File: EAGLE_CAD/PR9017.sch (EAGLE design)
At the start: 74 parts, among them SW1 C&K_PTS645, Y1 ABS25XTAL

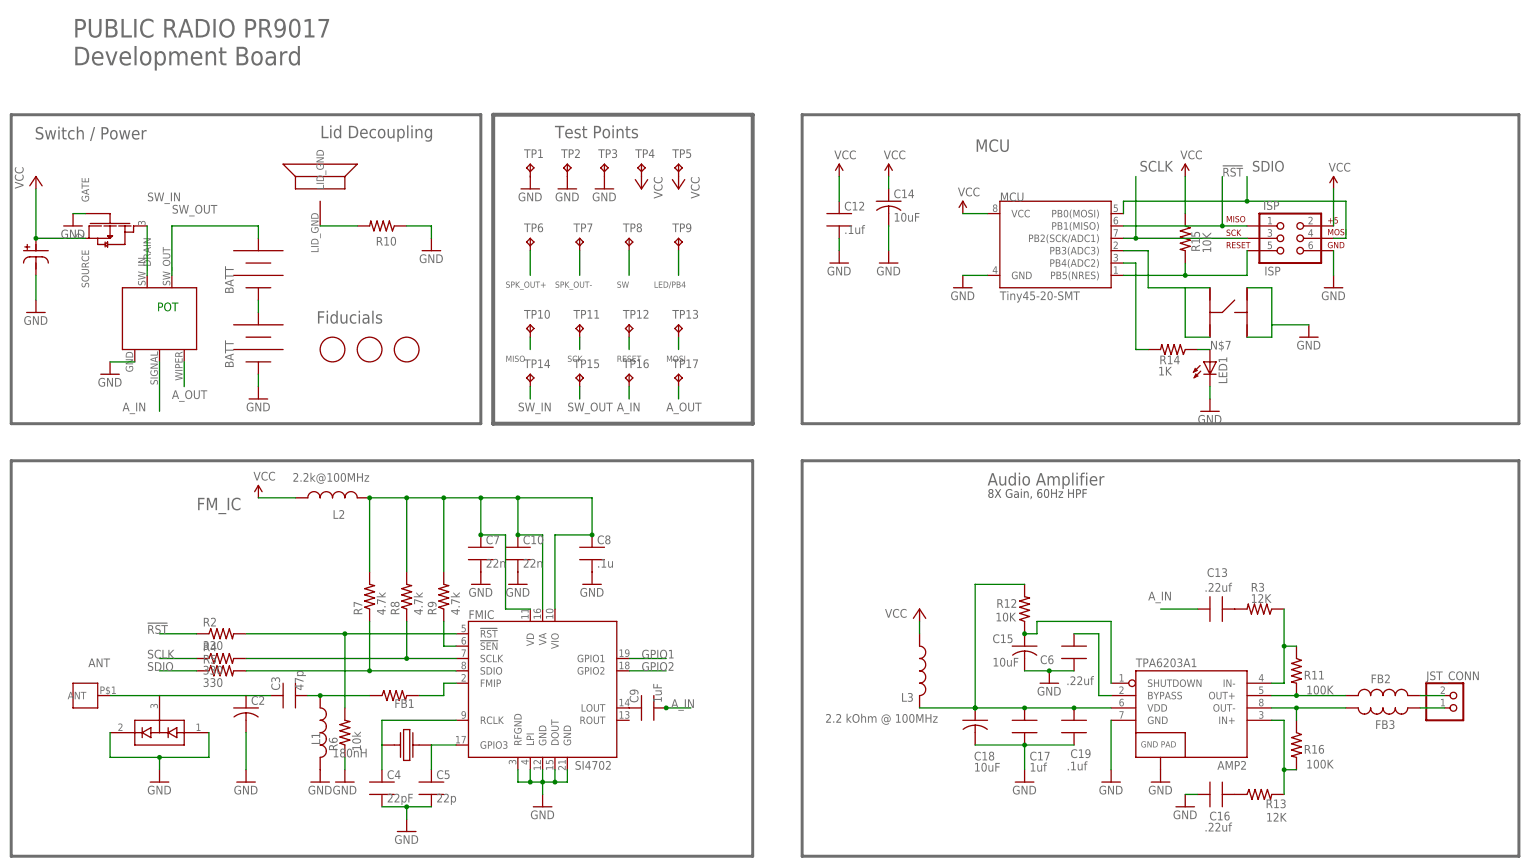
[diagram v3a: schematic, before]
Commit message: okay, woah
i spent a *ton* of time going through the partlist & BOM. at this point
basically everything in the circuit is from our PR_Parts_Library. i
also simplified & improved the package names, descriptions, etc. and i
gave all the passives 0603 footprints that came from the Common Parts
Library.

big thing: the values @ manufacturer part numbers. all of our parts
have a custom attribute called “MFG_PN”. we should go through EVERY
PART ON OUR SCHEMATIC and put actual manufacturer part numbers in those
fields. i did this for all the parts that seemed critical, but i didn’t
touch passives at all.

there’s also some other stuff that will matter on the BOM/partlist
side, but it’s probably best to just walk through in person or
digitally.

then: i went through all the parts and actually made them 0603.

then: i played with the FMIC area a bit. it’s not perfect but it’s a
start.

then: i started laying out the amp section. that’s definitely not done.
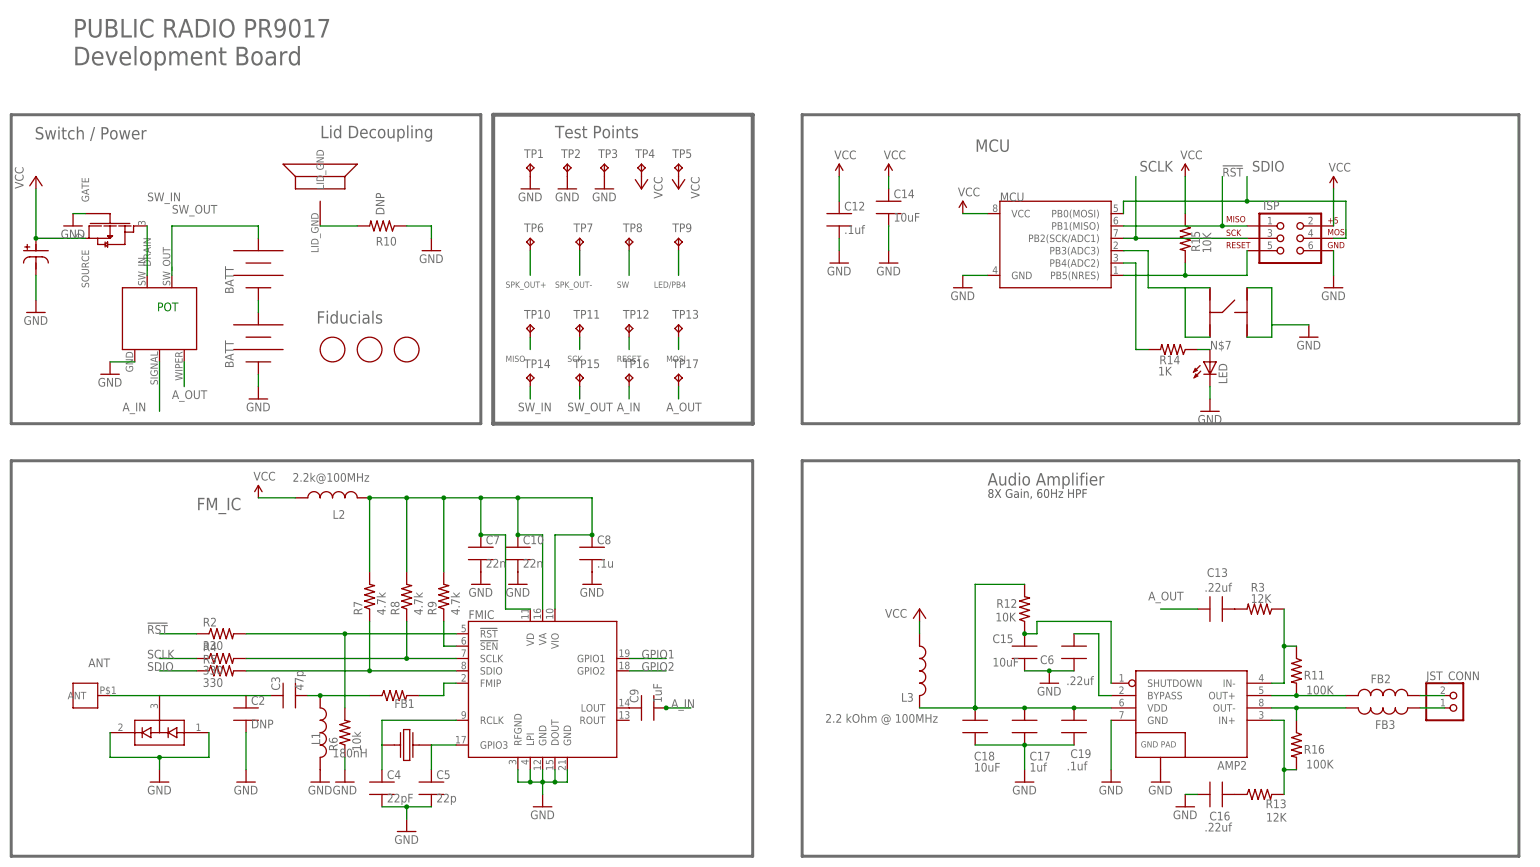
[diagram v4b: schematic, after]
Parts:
- removed LED1: (no value), led:LEDSML0603
- added LED: LED, PR_Parts_Library:LED
- ANT_MOUNT: value M3_SCREW_POST -> DNP
- C10, C12, C13, C16, C17, C19, C3, C4, C5, C6, C7, C8, C9: device PR_Parts_Library:CAP_SMT -> PR_Parts_Library:C_SMT_0603_CPL
- C14, C15, C18: device resistor:C-USC0603 -> PR_Parts_Library:C_SMT_0603_CPL
- C2: value (none) -> DNP; device resistor:C-USC0805 -> PR_Parts_Library:C_SMT_0603_CPL
- D1: device SparkFun-DiscreteSemi:BAV99 -> PR_Parts_Library:BAV99; MFG_PN (none) -> BAV99,215
- FB1, R6: device resistor:R-US_R0402 -> PR_Parts_Library:R_SMT_R0603_CPL
- FB2, FB3, L1: device SparkFun-Passives:INDUCTOR0805 -> PR_Parts_Library:L_SMT_0805_ADAFRUIT
- FET1: MFG_PN (none) -> AO3435
- FMIC: value SI4702 -> SI4702-C19-GMR; device PR_Parts_Library:SI470X -> PR_Parts_Library:SI4702-C19-GMR
- ISP: value ISP -> AVR_SPI_PRG_6NS; device SparkFun-Connectors:AVR_SPI_PRG_6NS -> PR_Parts_Library:AVR_SPI_PRG_6NS
- JST_CONN: device adafruit:JST_2PIN-SMT-RA -> PR_Parts_Library:JST_2PIN-SMT-RA
- L2, L3: device PR_Parts_Library:INDUCTOR -> PR_Parts_Library:L_SMT_0603_CPL
- MARK1, MARK2, MARK3: device adafruit:FIDUCIAL -> PR_Parts_Library:FIDUCIAL
- MCU: value Tiny45-20-SMT -> (none); device SparkFun-DigitalIC:ATTINY45TINY85-20-SMT -> PR_Parts_Library:ATTINY45TINY45-20-SMT
- R10: value (none) -> DNP; device resistor:R-US_R0805 -> PR_Parts_Library:R_SMT_R0603_CPL
- R11, R12, R13, R14, R15, R16, R2, R3, R4, R5, R7, R8, R9: device PR_Parts_Library:RES_SMT -> PR_Parts_Library:R_SMT_R0603_CPL
- SPKR_PLACE: value (none) -> DNP; device PR_Parts_Library:CE32A_FOR_JST -> PR_Parts_Library:PR2023_SPKR
- TP1, TP10, TP11, TP12, TP13, TP14, TP15, TP16, TP17, TP2, TP3, TP4, TP5, TP6, TP7, TP8, TP9: value TPTP20R -> (none); device testpad:TPTP20R -> PR_Parts_Library:TPTP20R
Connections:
- net A_IN: no longer C13.1
- net A_OUT: now also C13.1
- net GND: now also LED.C; no longer LED1.C
- net N$7: now also LED.A; no longer LED1.A

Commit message: Amp Updates
Changed the layout
-moved the decoupling as close as possible to the vd pin
-kept bypass cap also close by
-rerouted power
-removed the cap to ground on the shutdown pin from out previous
design, was not in place on any of the documentation for the 6203.
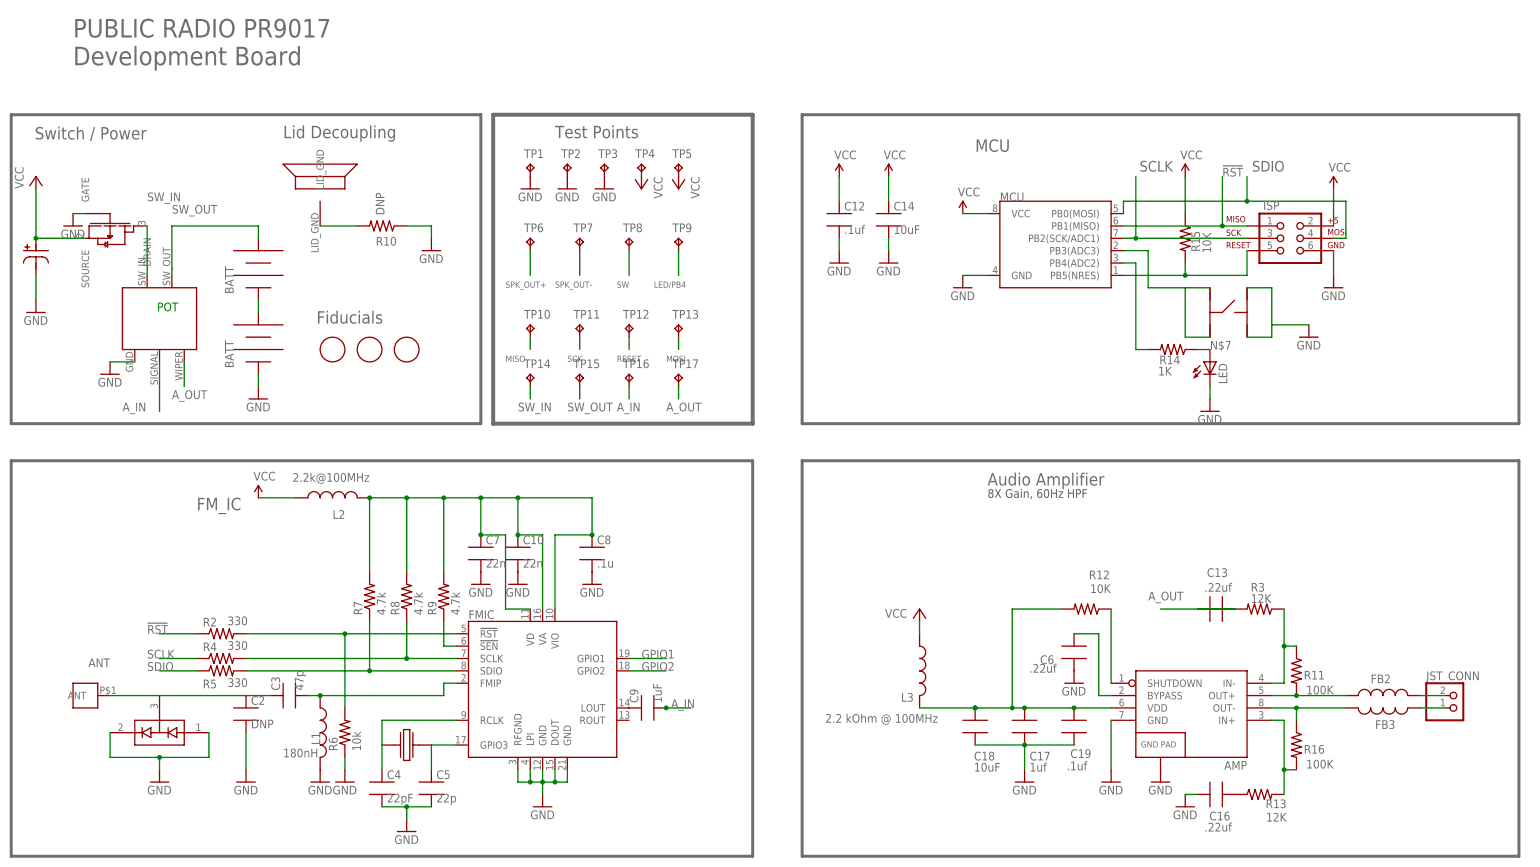
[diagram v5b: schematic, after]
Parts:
- removed C15: 10uF, PR_Parts_Library:C_SMT_0603_CPL
- removed FB1: (no value), PR_Parts_Library:R_SMT_R0603_CPL
- renumbered AMP2 to AMP
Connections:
- net A_OUT: now also C13.2; no longer C13.1
- net GND: no longer C15.2
- net N$16: no longer FB1.1
- net N$20: no longer C15.1
- net N$3: now also C13.1; no longer C13.2
- net N$6: no longer FB1.2
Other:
- moved on the sheet: C14, R12

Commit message: updated all part number etc
part number
added attributes for tolerance, voltage, power, etc
re routed FMIC per AN383
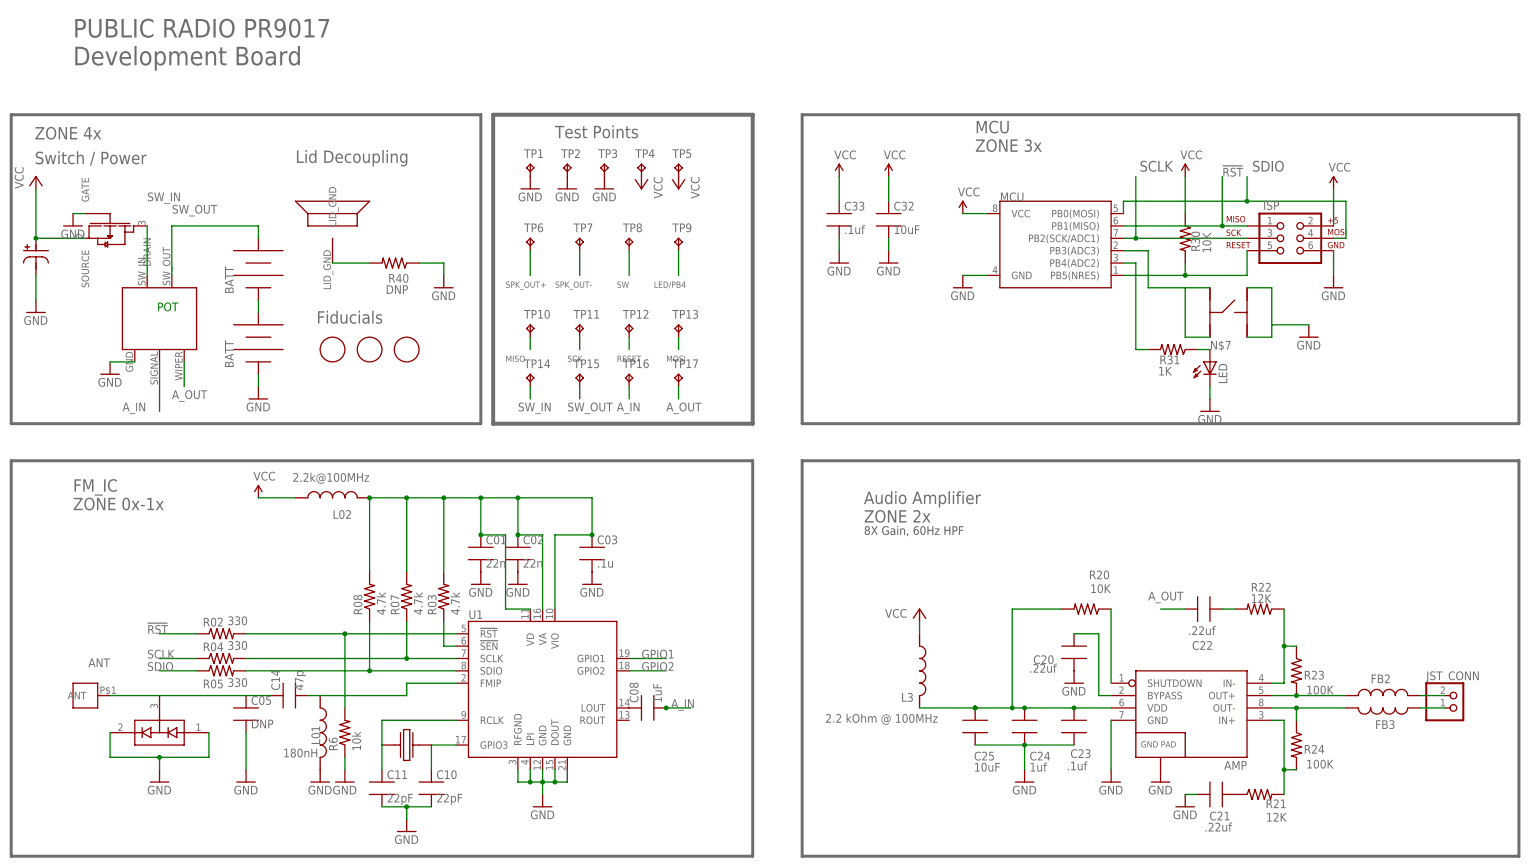
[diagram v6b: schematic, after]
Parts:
- removed C3: 47p, PR_Parts_Library:C_SMT_0603_CPL
- removed C5: 22p, PR_Parts_Library:C_SMT_0603_CPL
- removed R10: DNP, PR_Parts_Library:R_SMT_R0603_CPL
- added C02: 22n, PR_Parts_Library:C_SMT_0603_CPL
- added C32: 10uF, PR_Parts_Library:C_SMT_0603_CPL
- added R40: DNP, PR_Parts_Library:R_SMT_R0603_CPL
- C01, C03, C21, C22, C23, C33: TOL (none) -> 10%; VOLTAGE (none) -> 16V
- C05: TOL (none) -> 2%; VOLTAGE (none) -> 50V
- C08, C24: TOL (none) -> 10%; VOLTAGE (none) -> 10V
- C10: value 22n -> 22pF; TOL (none) -> 5%; VOLTAGE (none) -> 50V
- C11: TOL (none) -> 5%; VOLTAGE (none) -> 50V
- C14: value 10uF -> 47p
- C25: TOL (none) -> 20%; VOLTAGE (none) -> 6.3V
- C40: TOL (none) -> 20%; VOLTAGE (none) -> 16V
- FB2, FB3: CURRENT (none) -> 2A; DCR (none) -> 45m
- L01: CURRENT (none) -> 400mA; DCR (none) -> 640m; TOL (none) -> 5%
- L02: CURRENT (none) -> 150mA; DCR (none) -> 2.3
- L3: CURRENT (none) -> 150m; DCR (none) -> 2.3
- R02, R04, R05, R20, R30, R6: POWER (none) -> 1/10W; TOL (none) -> 5%
- R03, R07, R08, R31: POWER (none) -> 1/10W; TOL (none) -> 1%
- R21, R22, R23, R24: TOL (none) -> 1%
- renumbered C1 to C40, C12 to C33, C13 to C22, C16 to C21, C17 to C24, C18 to C25, C19 to C23, C2 to C05, C4 to C11, C6 to C20, C7 to C01, C8 to C03, C9 to C08, FMIC to U1, L1 to L01, L2 to L02, R11 to R23, R12 to R20, R13 to R21, R14 to R31, R15 to R30, R16 to R24, R2 to R02, R3 to R22, R4 to R04, R5 to R05, R7 to R08, R8 to R07, R9 to R03, Y1 to X1
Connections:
- removed net N$6: U1.FMIP
- net 3.3V: now also C02.1; no longer C10.1
- net ANT: now also C14.1; no longer C3.1
- net GND: now also C02.2, C32.2, R40.1; no longer C14.2, C5.2, R10.1
- net N$10: now also C10.1; no longer C5.1
- net N$16: now also C14.2, U1.FMIP; no longer C3.2
- net N$8: now also R40.2; no longer R10.2
- net VCC: now also C32.1; no longer C14.1
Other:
- note added: "Audio Amplifier ZONE 2x"
- note added: "FM_IC ZONE 0x-1x"
- note added: "MCU ZONE 3x"
- note added: "ZONE 4x"
- note removed: "Audio Amplifier"
- note removed: "FM_IC"
- note removed: "MCU"
- moved on the sheet: C10, C14

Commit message: BOM changes
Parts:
- C01, C02: value 22n -> 22nF
- C03: value .1u -> .1uF
- C14: value 47p -> 47pF
- C20, C21, C22: value .22uf -> .22uF
- C23, C33: value .1uf -> .1uF
- C24: value 1uf -> 1uF
- R03, R07, R08: value 4.7k -> 4.7K
- R6: value 10k -> 10K
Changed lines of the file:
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@@
 <attribute name="TOL" value="1%"/>
 </part>
-<part name="C22" library="PR_Parts_Library" deviceset="C_SMT" device="_0603_CPL" value=".22uf">
+<part name="C22" library="PR_Parts_Library" deviceset="C_SMT" device="_0603_CPL" value=".22uF">
 <attribute name="TOL" value="10%"/>
 <attribute name="VOLTAGE" value="16V"/>
 </part>
-<part name="C21" library="PR_Parts_Library" deviceset="C_SMT" device="_0603_CPL" value=".22uf">
+<part name="C21" library="PR_Parts_Library" deviceset="C_SMT" device="_0603_CPL" value=".22uF">
 <attribute name="TOL" value="10%"/>
 <attribute name="VOLTAGE" value="16V"/>
@@
 </part>
 <part name="GND16" library="SparkFun" deviceset="GND" device=""/>
-<part name="C33" library="PR_Parts_Library" deviceset="C_SMT" device="_0603_CPL" value=".1uf">
+<part name="C33" library="PR_Parts_Library" deviceset="C_SMT" device="_0603_CPL" value=".1uF">
 <attribute name="TOL" value="10%"/>
 <attribute name="VOLTAGE" value="16V"/>
 </part>
-<part name="C23" library="PR_Parts_Library" deviceset="C_SMT" device="_0603_CPL" value=".1uf">
+<part name="C23" library="PR_Parts_Library" deviceset="C_SMT" device="_0603_CPL" value=".1uF">
 <attribute name="TOL" value="10%"/>
 <attribute name="VOLTAGE" value="16V"/>
@@
 <attribute name="VOLTAGE" value="50V"/>
 </part>
-<part name="C14" library="PR_Parts_Library" deviceset="C_SMT" device="_0603_CPL" value="47p"/>
+<part name="C14" library="PR_Parts_Library" deviceset="C_SMT" device="_0603_CPL" value="47pF"/>
 <part name="C11" library="PR_Parts_Library" deviceset="C_SMT" device="_0603_CPL" value="22pF">
 <attribute name="TOL" value="5%"/>
@@
 <attribute name="VOLTAGE" value="50V"/>
 </part>
-<part name="C01" library="PR_Parts_Library" deviceset="C_SMT" device="_0603_CPL" value="22n">
+<part name="C01" library="PR_Parts_Library" deviceset="C_SMT" device="_0603_CPL" value="22nF">
 <attribute name="TOL" value="10%"/>
 <attribute name="VOLTAGE" value="16V"/>
 </part>
-<part name="C03" library="PR_Parts_Library" deviceset="C_SMT" device="_0603_CPL" value=".1u">
+<part name="C03" library="PR_Parts_Library" deviceset="C_SMT" device="_0603_CPL" value=".1uF">
 <attribute name="TOL" value="10%"/>
 <attribute name="VOLTAGE" value="16V"/>
@@
 <attribute name="TOL" value="5%"/>
 </part>
-<part name="R07" library="PR_Parts_Library" deviceset="R_SMT" device="_R0603_CPL" value="4.7k">
+<part name="R07" library="PR_Parts_Library" deviceset="R_SMT" device="_R0603_CPL" value="4.7K">
 <attribute name="POWER" value="1/10W"/>
 <attribute name="TOL" value="1%"/>
 </part>
-<part name="R03" library="PR_Parts_Library" deviceset="R_SMT" device="_R0603_CPL" value="4.7k">
+<part name="R03" library="PR_Parts_Library" deviceset="R_SMT" device="_R0603_CPL" value="4.7K">
 <attribute name="POWER" value="1/10W"/>
 <attribute name="TOL" value="1%"/>
 </part>
-<part name="R08" library="PR_Parts_Library" deviceset="R_SMT" device="_R0603_CPL" value="4.7k">
+<part name="R08" library="PR_Parts_Library" deviceset="R_SMT" device="_R0603_CPL" value="4.7K">
 <attribute name="POWER" value="1/10W"/>
 <attribute name="TOL" value="1%"/>
 </part>
-<part name="R6" library="PR_Parts_Library" deviceset="R_SMT" device="_R0603_CPL" value="10k">
+<part name="R6" library="PR_Parts_Library" deviceset="R_SMT" device="_R0603_CPL" value="10K">
 <attribute name="POWER" value="1/10W"/>
 <attribute name="TOL" value="5%"/>
 </part>
-<part name="C02" library="PR_Parts_Library" deviceset="C_SMT" device="_0603_CPL" value="22n">
+<part name="C02" library="PR_Parts_Library" deviceset="C_SMT" device="_0603_CPL" value="22nF">
 <attribute name="TOL" value="10%"/>
 <attribute name="VOLTAGE" value="16V"/>
@@
 <attribute name="VOLTAGE" value="6.3V"/>
 </part>
-<part name="C24" library="PR_Parts_Library" deviceset="C_SMT" device="_0603_CPL" value="1uf">
+<part name="C24" library="PR_Parts_Library" deviceset="C_SMT" device="_0603_CPL" value="1uF">
 <attribute name="TOL" value="10%"/>
 <attribute name="VOLTAGE" value="10V"/>
@@
 <part name="TP16" library="PR_Parts_Library" deviceset="TP" device="TP20R"/>
 <part name="TP17" library="PR_Parts_Library" deviceset="TP" device="TP20R"/>
-<part name="C20" library="PR_Parts_Library" deviceset="C_SMT" device="_0603_CPL" value=".22uf"/>
+<part name="C20" library="PR_Parts_Library" deviceset="C_SMT" device="_0603_CPL" value=".22uF"/>
 <part name="GND15" library="SparkFun-Aesthetics" deviceset="GND" device=""/>
 <part name="R22" library="PR_Parts_Library" deviceset="R_SMT" device="_R0603_CPL" value="12K">

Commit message: added MFG_PN for everything
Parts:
- C01, C02: MFG_PN (none) -> CL10B223KB8NNNC
- C03, C23, C33: MFG_PN (none) -> CL05B104KO5NNNC
- C05: MFG_PN (none) -> DNP
- C08, C24: MFG_PN (none) -> CL10B105KP8NNNC
- C10, C11: MFG_PN (none) -> C1608C0G1H220J080AA
- C14: MFG_PN (none) -> CL10C470JB8NCNC; TOL (none) -> 5%; VOLTAGE (none) -> 50V
- C20: MFG_PN (none) -> C1608X7R1C224K080AC; TOL (none) -> 10%; VOLTAGE (none) -> 16V
- C21, C22: MFG_PN (none) -> C1608X7R1C224K080AC
- C25, C32: MFG_PN (none) -> CL10A106MQ8NNNC
- FB2, FB3: MFG_PN (none) -> HI0805R800R-10
- L01: MFG_PN (none) -> AISC-0805-R18J-T
- L02: MFG_PN (none) -> HZ0603A222R-10
- L03: value 2.2 kOhm @ 100MHz -> 2.2k@100MHz; CURRENT 150m -> 150mA; MFG_PN (none) -> HZ0603A222R-10
- R02, R04, R05: MFG_PN (none) -> MCR03ERTJ331
- R03, R07, R08: MFG_PN (none) -> ERJ-3EKF4701V
- R20, R30, R6: MFG_PN (none) -> ERJ-3GEYJ103V
- R21, R22: MFG_PN (none) -> RMCF0603FT12K0; POWER (none) -> 1/10W
- R23, R24: MFG_PN (none) -> RMCF0603FT100K; POWER (none) -> 1/10W
- R31: MFG_PN (none) -> ERJ-3EKF1001V
- R40: MFG_PN (none) -> ERJ-3GEY0R00V
- renumbered L3 to L03
